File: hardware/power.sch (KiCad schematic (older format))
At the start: 62 parts

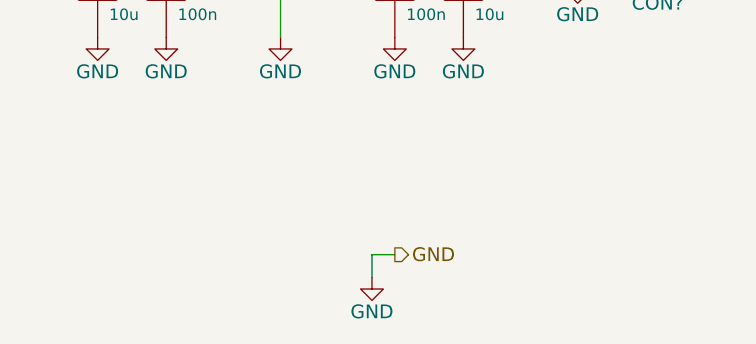
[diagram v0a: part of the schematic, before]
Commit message: Remove GND label from power supply
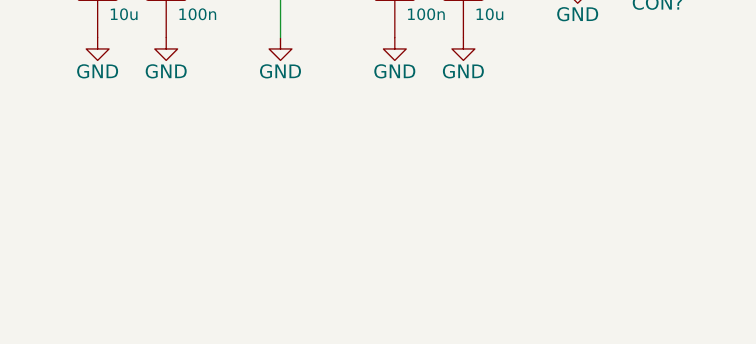
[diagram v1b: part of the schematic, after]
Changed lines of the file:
@@
 Text HLabel 6500 3800 2    60   Output ~ 0
 -6V_VCA
-Text HLabel 9200 5800 2    60   Output ~ 0
-GND
 Text HLabel 6150 5300 2    60   Output ~ 0
 9V_Wah
@@
 Connection ~ 6300 3800
 $Comp
-L GND #PWR?
-U 1 1 54D4F5A1
-P 9100 5900
-F 0 "#PWR?" H 9100 5650 60  0001 C CNN
-F 1 "GND" H 9100 5750 60  0000 C CNN
-F 2 "" H 9100 5900 60  0000 C CNN
-F 3 "" H 9100 5900 60  0000 C CNN
-	1    9100 5900
-	1    0    0    -1
-$EndComp
-Wire Wire Line
-	9100 5900 9100 5800
-Wire Wire Line
-	9100 5800 9200 5800
-$Comp
 L LM7809CT U?

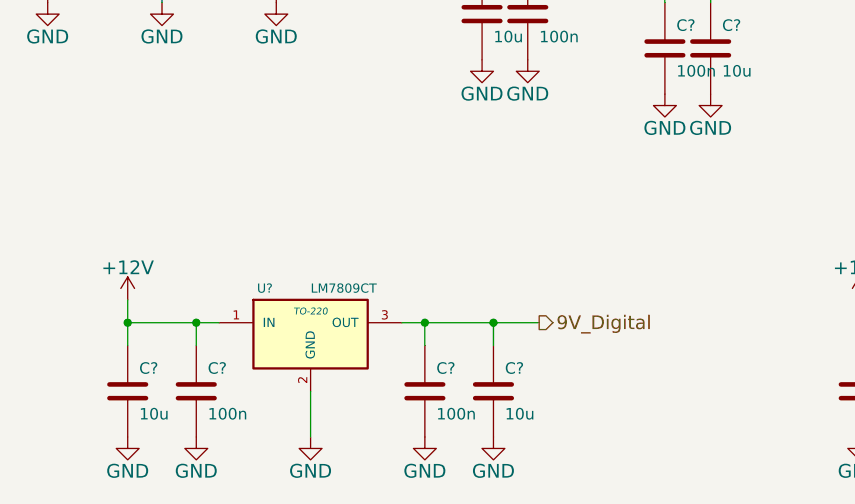
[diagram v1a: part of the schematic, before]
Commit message: Use global label for digital (noisy) 9V
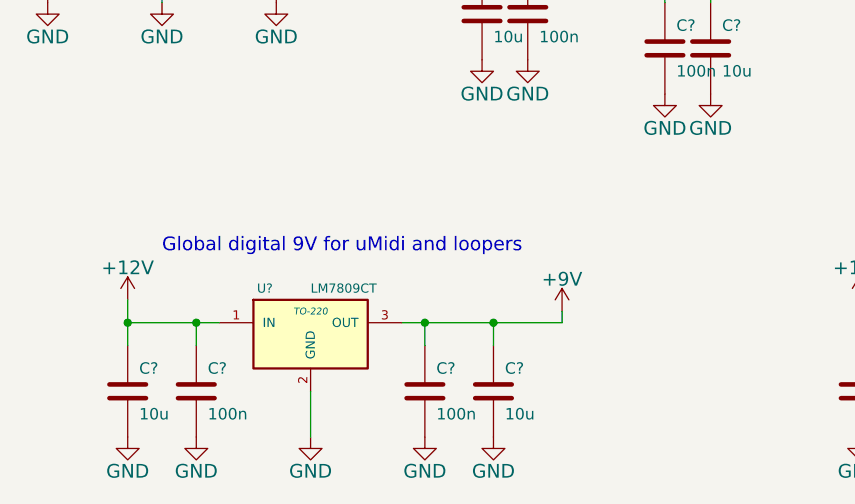
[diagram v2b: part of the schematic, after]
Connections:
- net 9V_Digital renamed +9V
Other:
- note added: "Global digital 9V for uMidi and loopers"
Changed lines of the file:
@@
 Text HLabel 6150 5300 2    60   Output ~ 0
 9V_Wah
-Text HLabel 2950 5300 2    60   Output ~ 0
-9V_Digital
 $Comp
 L BARREL_JACK CON?
@@
 	1950 5800 1950 5600
 Wire Wire Line
-	2350 5300 2950 5300
+	2350 5300 3050 5300
 $Comp
 L LM7809CT U?
@@
 Wire Wire Line
 	5550 5300 6150 5300
+$Comp
+L +9V #PWR?
+U 1 1 54E93105
+P 3050 5250
+F 0 "#PWR?" H 3050 5100 60  0001 C CNN
+F 1 "+9V" H 3050 5390 60  0000 C CNN
+F 2 "" H 3050 5250 60  0000 C CNN
+F 3 "" H 3050 5250 60  0000 C CNN
+	1    3050 5250
+	1    0    0    -1
+$EndComp
+Wire Wire Line
+	3050 5300 3050 5250
+Text Notes 1300 5000 0    60   ~ 0
+Global digital 9V for uMidi and loopers
 $EndSCHEMATC
